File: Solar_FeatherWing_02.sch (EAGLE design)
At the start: 39 parts, among them IC1 SPV1040T, IC2 TPL5111, J1 1X2-3.5MM, SW2 SW-K3-1290S-J1

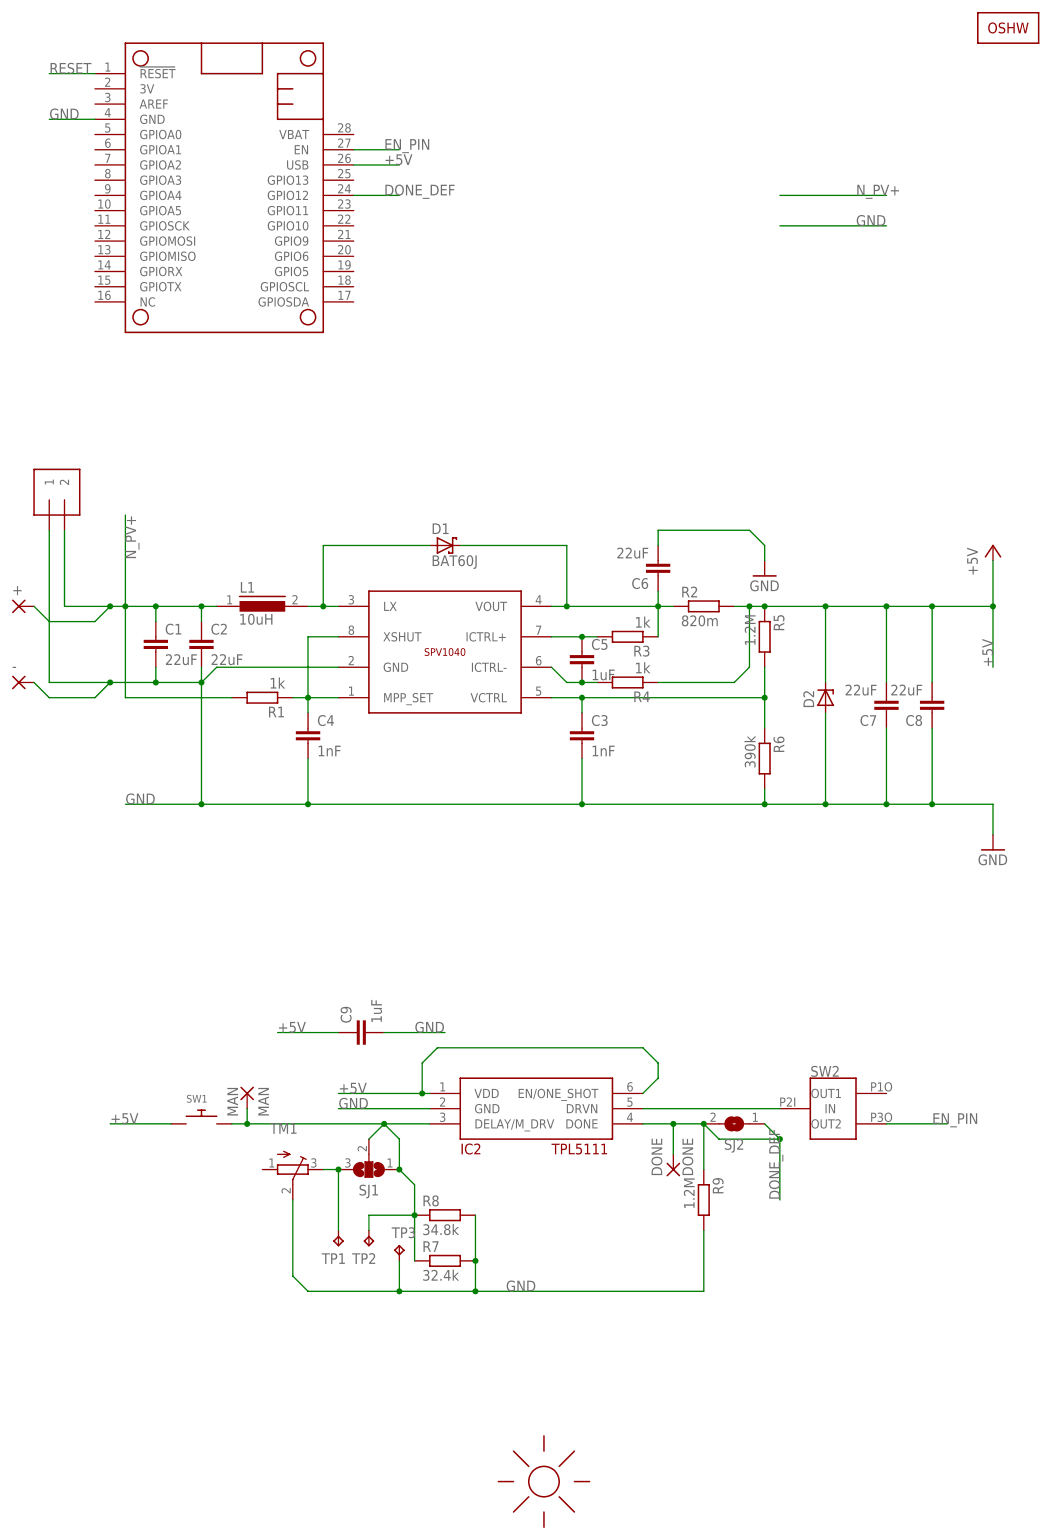
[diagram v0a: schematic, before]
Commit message: Changed features
Removed the timer-ic and added a INA219 to monitor power.
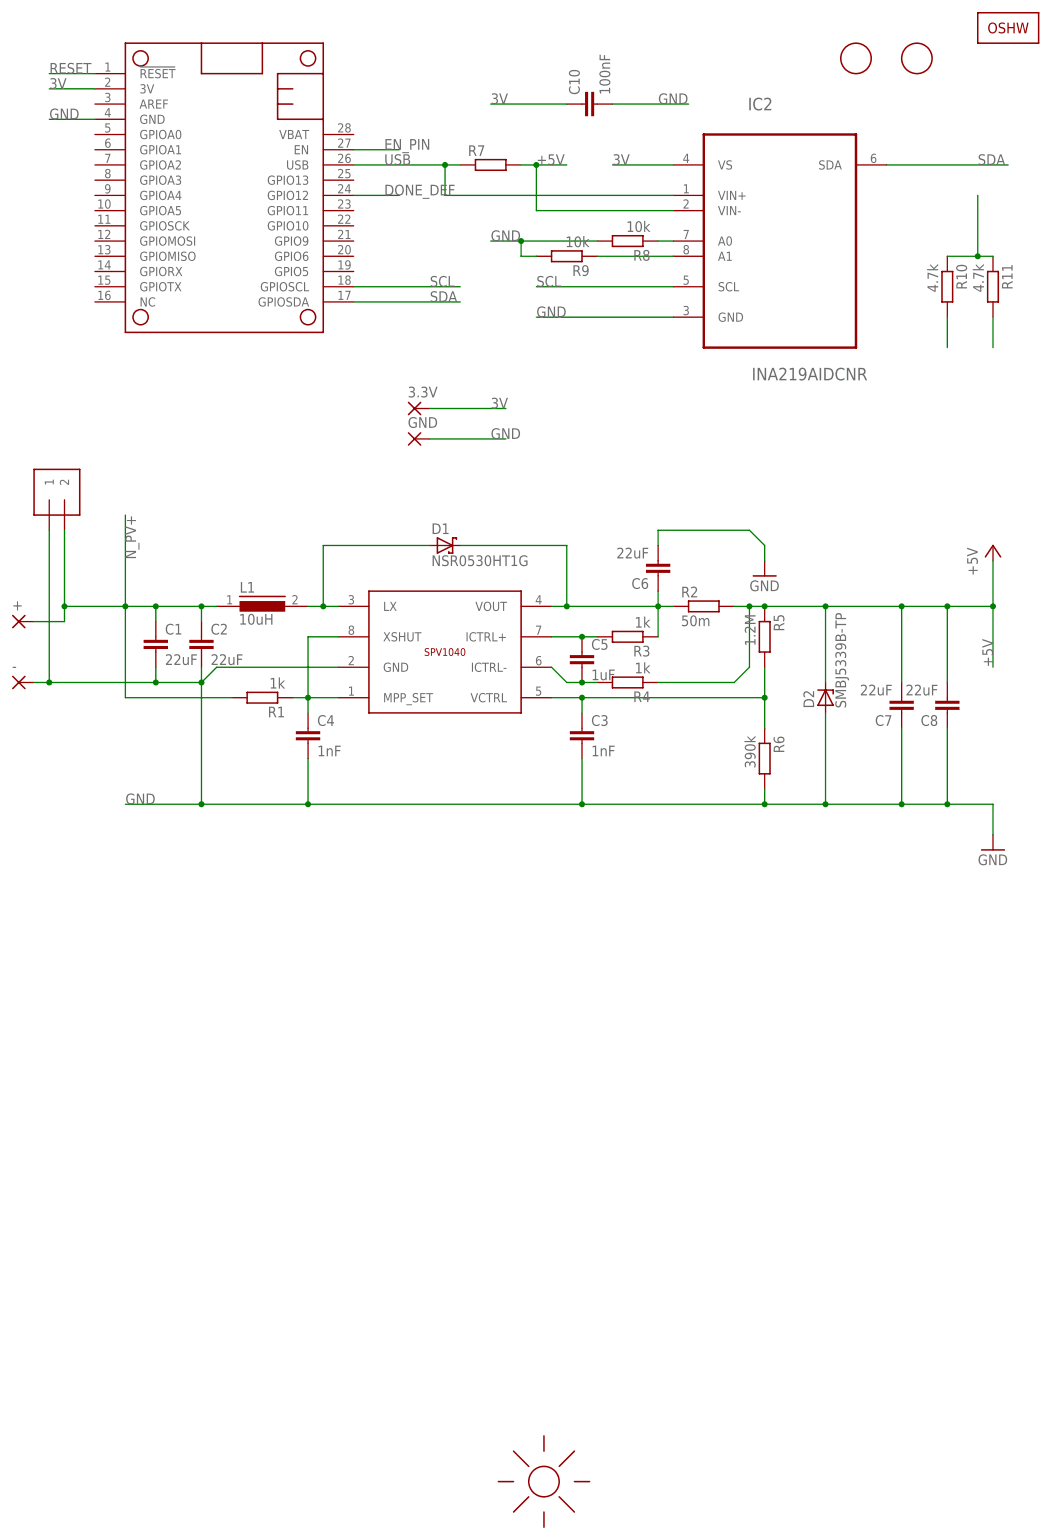
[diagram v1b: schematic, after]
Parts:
- removed C9: 1uF, rcl:C-EUC0603K
- removed DONE: DONE, wirepad:1,6/0,9
- removed MAN: MAN, wirepad:1,6/0,9
- removed SJ1: JUMPER3-0603-NC, we-rcl:JUMPER3-0603-NC
- removed SJ2: JUMPER2-0603-NC, we-rcl:JUMPER2-0603-NC
- removed SW1: (no value), adafruit:SWITCH_PUSHBUTTONC&K_KSS
- removed SW2: SW-K3-1290S-J1, _RTC-Lib:SW-K3-1290S-J1
- removed TM1: (no value), adafruit:TRIMPOTTC33X
- removed TP1, TP2, TP3: TPB1,27, testpad:TPB1,27
- added 3.3V, GND: (no value), wirepad:1,6/0,9
- added C10: 100nF, rcl:C-EUC0603K
- added R10, R11: 4.7k, rcl:R-EU_R0603
- added U$2, U$3: FIDUCIAL, adafruit:FIDUCIAL
- D1: value BAT60J -> NSR0530HT1G
- D2: value (none) -> SMBJ5339B-TP
- IC2: value TPL5111 -> INA219AIDCNR; device _RTC-Lib:TPL5111 -> Texas Instruments_By_element14_Batch_1:INA219AIDCNR
- R2: value 820m -> 50m
- R7: value 32.4k -> (none); device rcl:R-EU_R0603 -> rcl:R-EU_R1206
- R8: value 34.8k -> 10k
- R9: value 1.2M -> 10k
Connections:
- removed net N$6: IC2.DRVN, SW2.IN
- removed net N$8: SJ1.3, TM1.E, TP1.TP
- removed net N$9: IC2.DELAY/M_DRV, MAN.P, R7.1, R8.1, SJ1.1, SJ1.2, SW1.P$2, TP2.TP
- new net 3V: 3.3V.P, C10.1, IC2.VS, MS1.3V, R10.1, R11.1
- new net N$35: IC2.A1, R9.1
- new net N$36: IC2.A0, R8.1
- new net SCL: IC2.SCL, MS1.GPIOSCL, R11.2
- new net SDA: IC2.SDA, MS1.GPIOSDA, R10.2
- new net USB: IC2.VIN+, MS1.USB, R7.1
- net +5V: now also IC2.VIN-, R7.2; no longer C9.1, IC2.EN/ONE_SHOT, IC2.VDD, MS1.USB, SW1.P$1
- net DONE_DEF: no longer DONE.P, IC2.DONE, R9.1, SJ2.1, SJ2.2
- net EN_PIN: no longer SW2.OUT2
- net GND: now also C10.2, GND.P; no longer C9.2, R7.2, TM1.S, TP3.TP
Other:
- moved on the sheet: +, C7, C8, R7, R8, R9

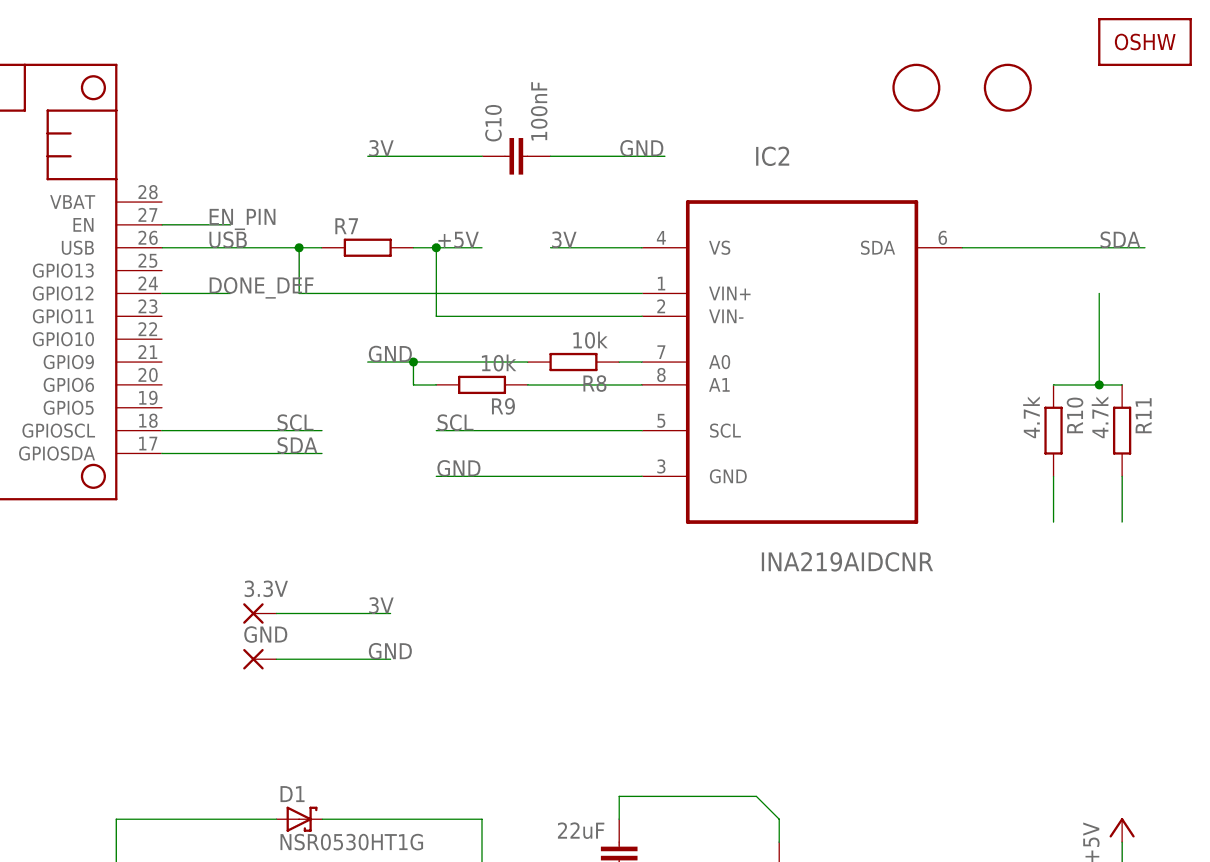
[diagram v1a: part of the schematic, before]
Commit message: Monitor battery current and voltage
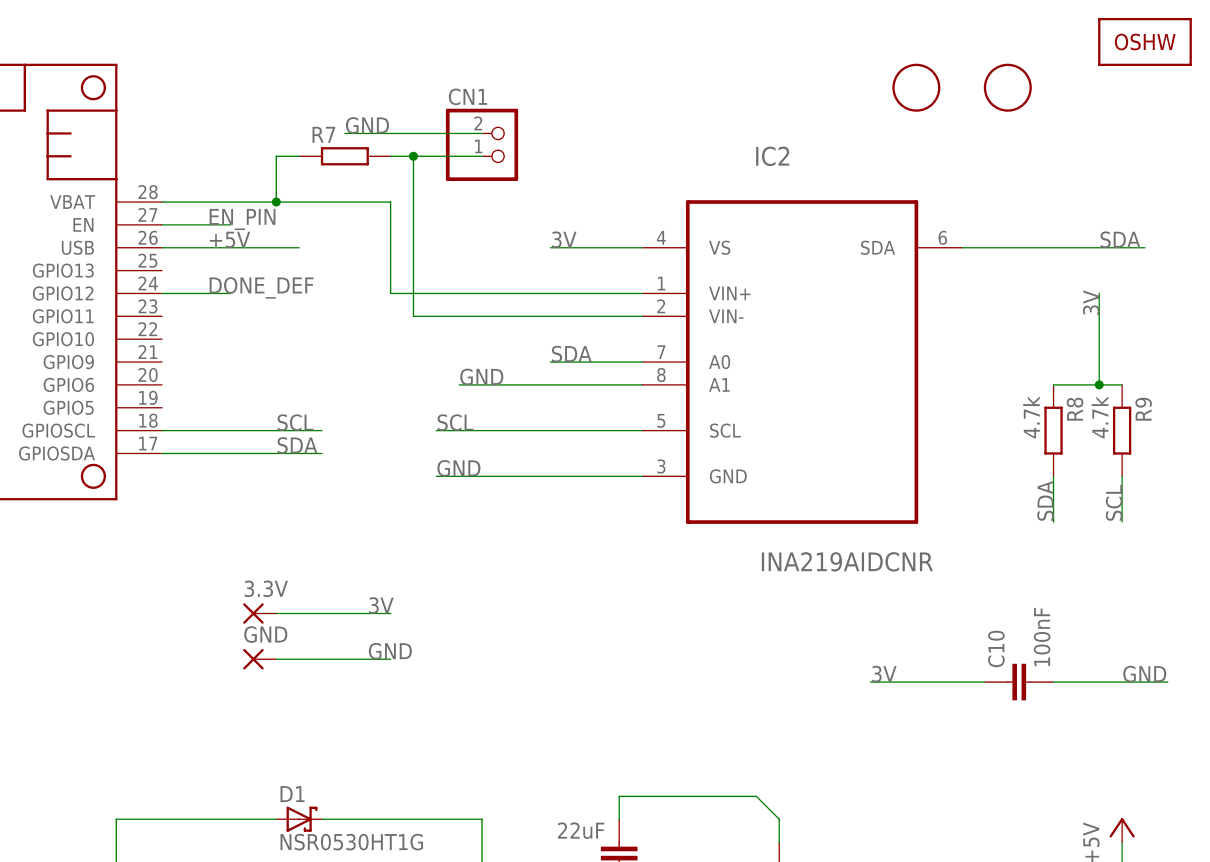
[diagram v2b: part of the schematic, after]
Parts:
- removed R10, R11: 4.7k, rcl:R-EU_R0603
- added CN1: (no value), adafruit:JST_2PIN-SMT-RA
- R8, R9: value 10k -> 4.7k
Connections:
- removed net N$35: IC2.A1, R9.1
- removed net N$36: IC2.A0, R8.1
- removed net USB: IC2.VIN+, MS1.USB, R7.1
- new net N$15: CN1.2, IC2.VIN-, R7.2
- new net VBAT: IC2.VIN+, MS1.VBAT, R7.1
- net +5V: now also MS1.USB; no longer IC2.VIN-, R7.2
- net 3V: now also R8.1, R9.1; no longer R10.1, R11.1
- net GND: now also CN1.1, IC2.A1; no longer R8.2, R9.2
- net SCL: now also R9.2; no longer R11.2
- net SDA: now also IC2.A0, R8.2; no longer R10.2
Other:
- moved on the sheet: C10, R7, R8, R9
